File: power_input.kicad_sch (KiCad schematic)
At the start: 47 parts, among them IC10 MAX17263LETD+T, IC2 MCP73871, IC4 TPS2013A, IC7 LP38691-ADJ, J2 JST_4PIN

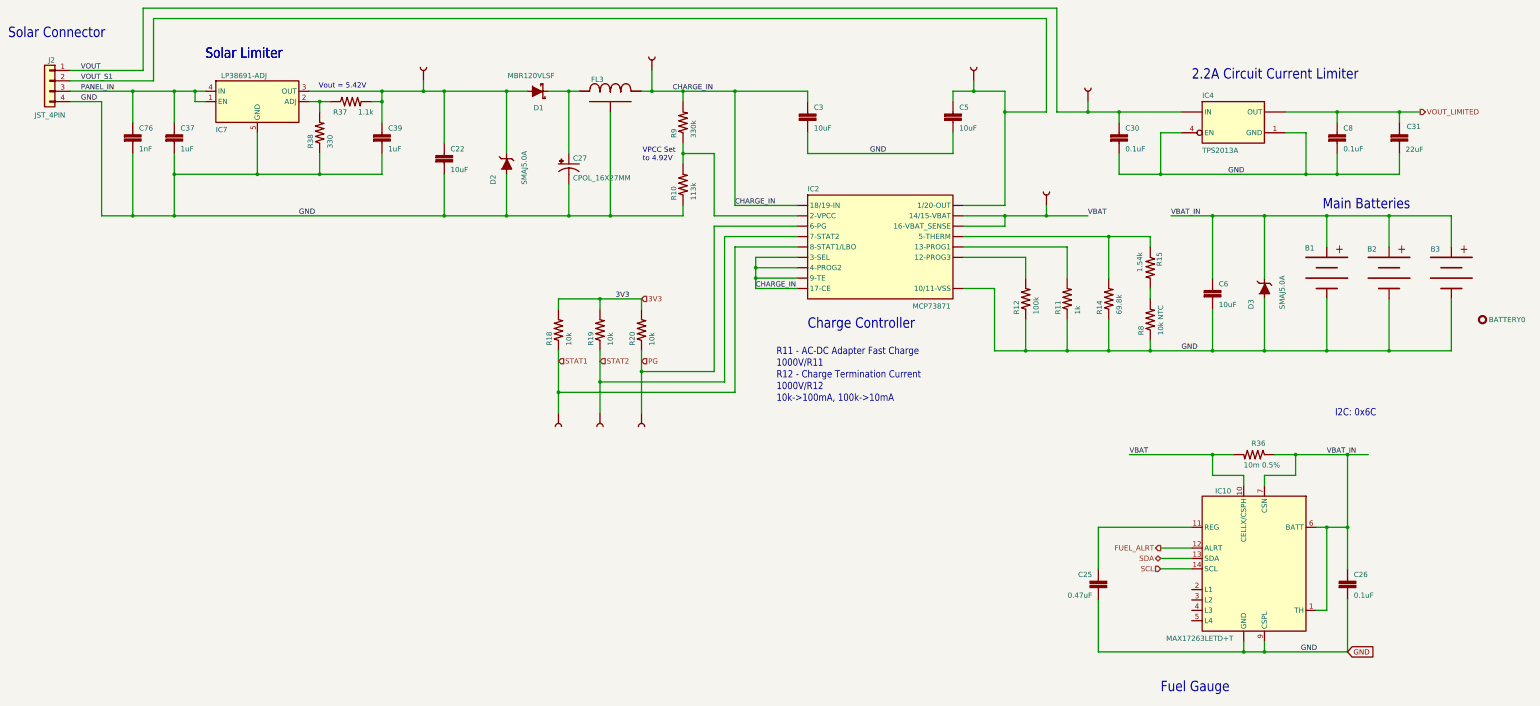
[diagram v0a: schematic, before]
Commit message: name change to Loriques
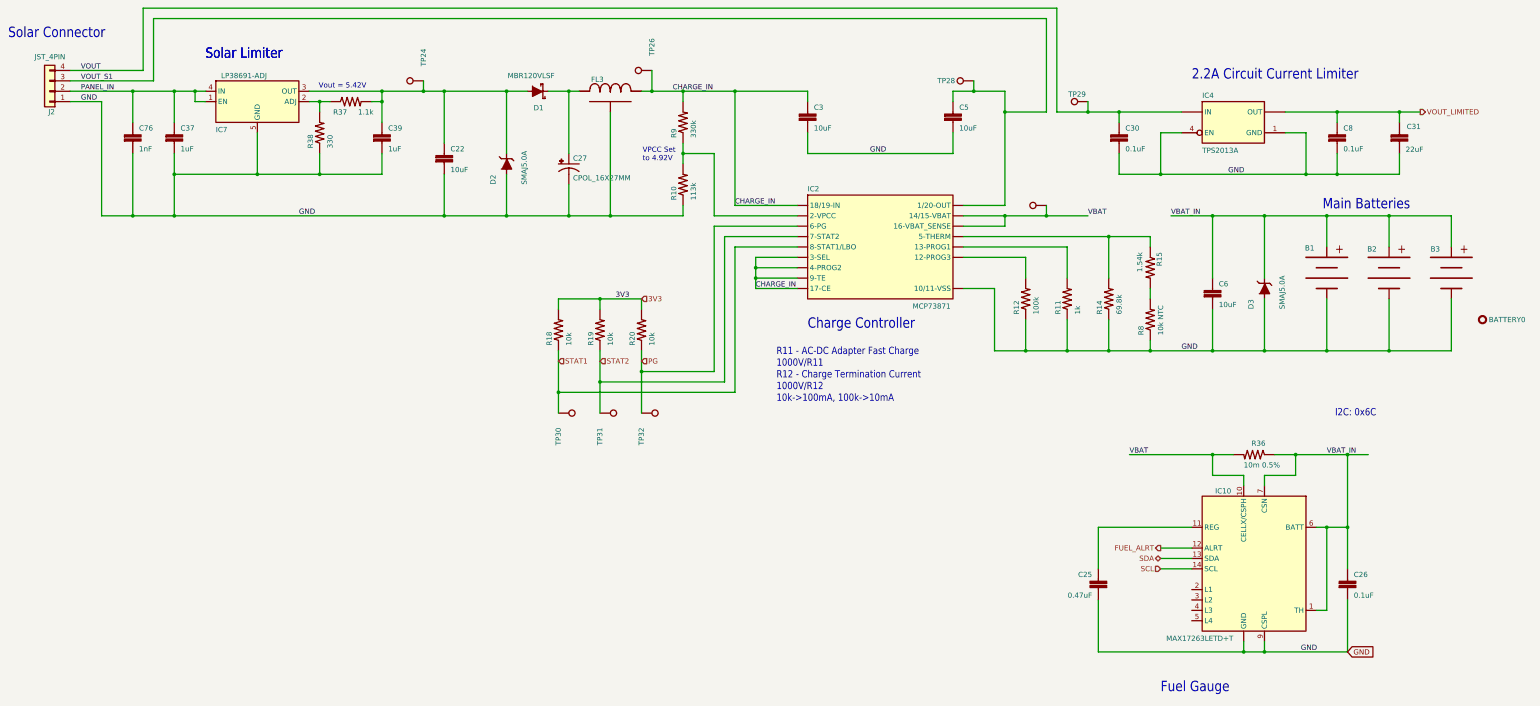
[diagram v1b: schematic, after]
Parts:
- B1, B2, B3: footprint autonode:1042 -> Loriques:1042; symbol autonode:18650_1042 -> Loriques:18650_1042
- BATTERY0: footprint autonode:NOTHING -> Loriques:NOTHING; symbol autonode:BULLET -> Loriques:BULLET
- C22, C3, C5, C6: symbol autonode:CAP0603 -> Loriques:CAP0603
- C25, C26, C30, C37, C39, C76, C8: symbol autonode:CAP0402 -> Loriques:CAP0402
- C27: footprint autonode:25PK4700MEFC16X25 -> Loriques:25PK4700MEFC16X25; symbol autonode:CPOL_16X27MM -> Loriques:CPOL_16X27MM
- C31: symbol autonode:CAP0805 -> Loriques:CAP0805
- D1: footprint autonode:SOD−123FL -> Loriques:SOD−123FL; symbol autonode:MBR120VLSF -> Loriques:MBR120VLSF
- D2, D3: footprint autonode:DO-214AC(SMA) -> Loriques:DO-214AC(SMA); symbol autonode:SMAJ5.0A -> Loriques:SMAJ5.0A
- FL3: footprint autonode:YFF31HC2A104MT000N -> Loriques:YFF31HC2A104MT000N; symbol autonode:YFF31HC2A104MT000N -> Loriques:YFF31HC2A104MT000N
- IC10: footprint autonode:SON40P300X300X80-15T170X230N -> Loriques:SON40P300X300X80-15T170X230N; symbol autonode:MAX17263LETD+T -> Loriques:MAX17263LETD+T
- IC2: footprint autonode:QFN20-ML_4X4MM -> Loriques:QFN20-ML_4X4MM; symbol autonode:MCP73871 -> Loriques:MCP73871
- IC4: footprint autonode:R-PDSO-G8_NOPAD -> Loriques:R-PDSO-G8_NOPAD; symbol autonode:TPS2013A -> Loriques:TPS2013A
- IC7: footprint autonode:SOT-223-5 -> Loriques:SOT-223-5; symbol autonode:LP38691-ADJ -> Loriques:LP38691-ADJ
- J2: footprint autonode:JST-PH-4-SMT -> Loriques:JST-PH-4-SMT
- R10, R11, R12, R14, R15, R18, R19, R20, R37, R38, R8, R9: symbol autonode:RESISTOR0402-RES -> Loriques:RESISTOR0402-RES
- R36: symbol autonode:RESISTOR1206 -> Loriques:RESISTOR1206
- TP24, TP26, TP27, TP28, TP29, TP30, TP31, TP32: footprint autonode:PAD.03X.05 -> TestPoint:TestPoint_Pad_D1.5mm; symbol autonode:TEST-POINT3X5 -> Connector:TestPoint
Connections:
- net CHARGE_IN: now also TP26.1; no longer TP26.0 (1)
- net GND: now also J2.1 (Pin_1); no longer J2.4 (Pin_4)
- net PANEL_IN: now also J2.2 (Pin_2); no longer J2.3 (Pin_3)
- net PG: now also TP32.1; no longer TP32.0 (1)
- net STAT1: now also TP30.1; no longer TP30.0 (1)
- net STAT2: now also TP31.1; no longer TP31.0 (1)
- net VBAT: now also TP27.1; no longer TP27.0 (1)
- net VOUT: now also J2.4 (Pin_4), TP29.1; no longer J2.1 (Pin_1), TP29.0 (1)
- net VOUT_S1: now also J2.3 (Pin_3), TP28.1; no longer J2.2 (Pin_2), TP28.0 (1)
- net at C22.1, C39.1, D1.A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: now also TP24.1; no longer TP24.0 (1)
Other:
- moved on the sheet: J2

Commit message: added logo to schematic sheets
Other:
- title: (none) -> Loriques
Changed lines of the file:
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@@
 	(generator "eeschema")
 	(generator_version "9.0")
-	(paper "User" 411.302 254.991)
+	(paper "A3")
+	(title_block
+		(title "Loriques")
+		(date "2025-07-11")
+		(rev "A")
+	)
 	(text "Vout = 5.42V"
 		(exclude_from_sim no)

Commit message: added lots of 3d models
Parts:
- C27: footprint Loriques:25PK4700MEFC16X25 -> Capacitor_THT:CP_Radial_D16.0mm_P7.50mm; DK (none) -> 1189-1732-ND; PARTNO (none) -> 25PK4700MEFC16X25
- J2: DK (none) -> 455-B4B-PH-SM4-TBCT-ND; PARTNO (none) -> B4B-PH-SM4-TB
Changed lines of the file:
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@@
 			)
 		)
-		(property "Footprint" "Loriques:25PK4700MEFC16X25"
+		(property "Footprint" "Capacitor_THT:CP_Radial_D16.0mm_P7.50mm"
 			(at 154.94 104.14 0)
 			(effects
@@
 		)
 		(property "Description" "4700µF 25V Aluminum Electrolytic Capacitors Radial"
+			(at 154.94 104.14 0)
+			(effects
+				(font
+					(size 1.27 1.27)
+				)
+				(hide yes)
+			)
+		)
+		(property "PARTNO" "25PK4700MEFC16X25"
+			(at 154.94 104.14 0)
+			(effects
+				(font
+					(size 1.27 1.27)
+				)
+				(hide yes)
+			)
+		)
+		(property "DK" "1189-1732-ND"
 			(at 154.94 104.14 0)
 			(effects
@@
 			(at 27.94 86.36 0)
 			(effects
+				(font
+					(size 1.27 1.27)
+				)
+				(hide yes)
+			)
+		)
+		(property "PARTNO" "B4B-PH-SM4-TB"
+			(at 27.94 86.36 0)
+			(effects
+				(font
+					(size 1.27 1.27)
+				)
+				(hide yes)
+			)
+		)
+		(property "DK" "455-B4B-PH-SM4-TBCT-ND"
+			(at 27.94 86.36 0)
+			(effects

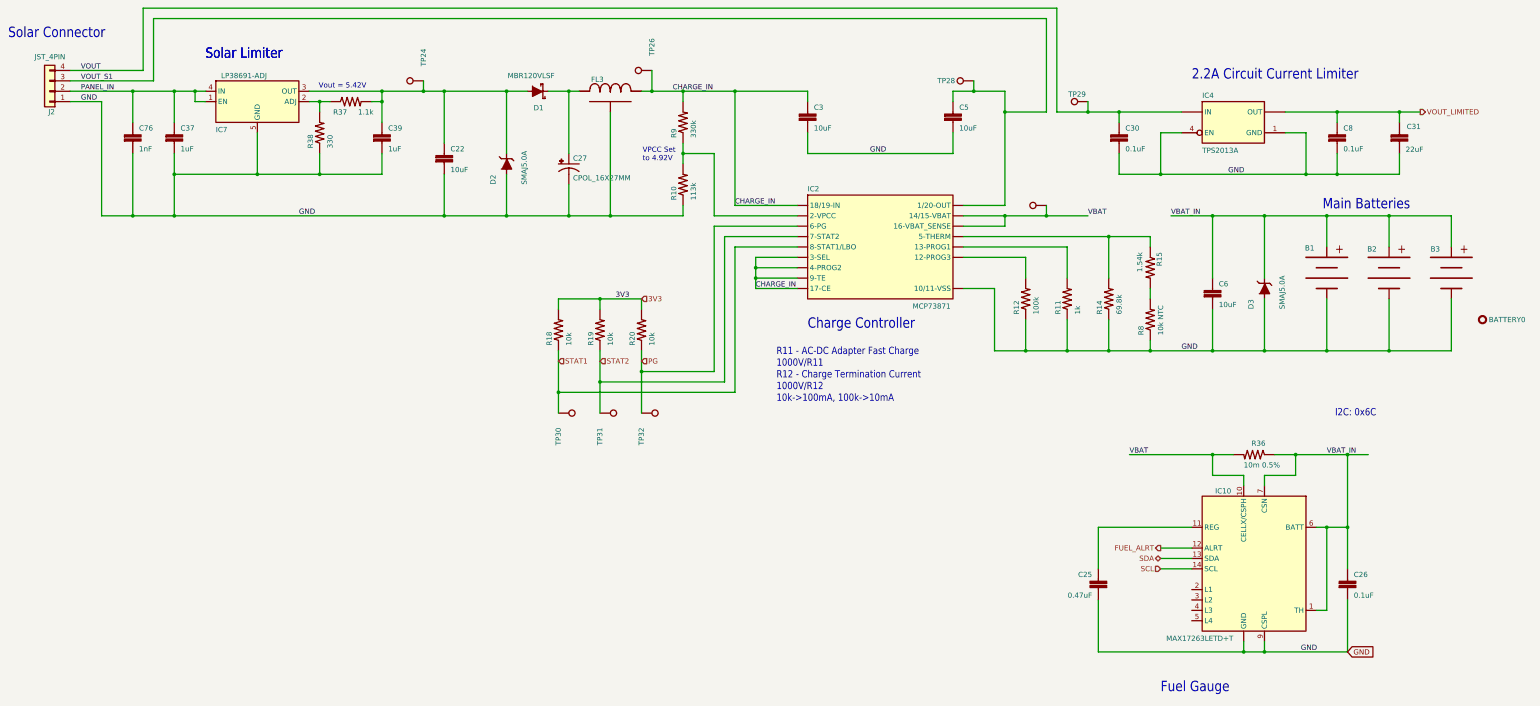
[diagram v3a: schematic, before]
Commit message: more 3D parts. changed out the temp/humidity sensor for an instock one
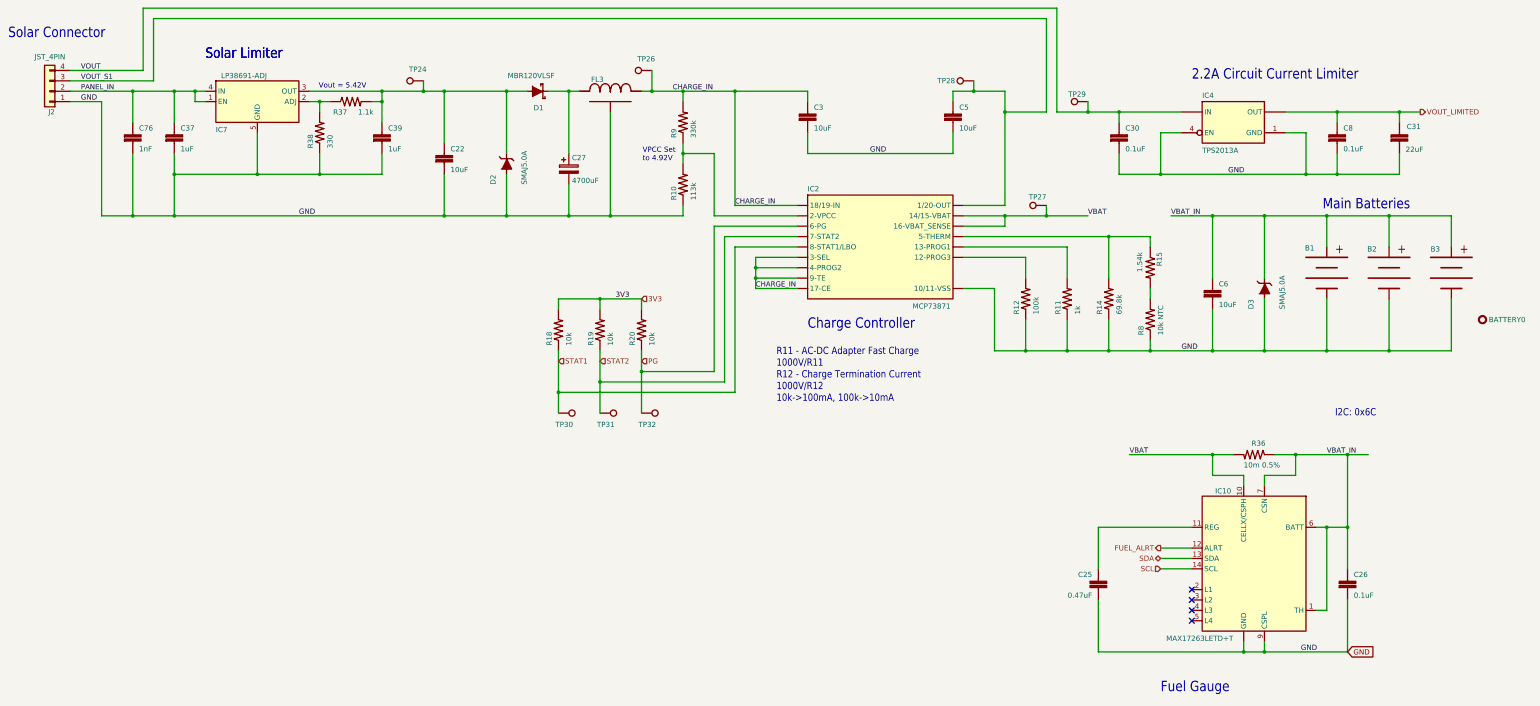
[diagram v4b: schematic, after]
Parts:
- C27: value CPOL_16X27MM -> 4700uF; symbol Loriques:CPOL_16X27MM -> Device:C_Polarized
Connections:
- net GND: now also C27.2; no longer C27.-
- net at D1.K, FL3.1: now also C27.1; no longer C27.+
- no-connect marks 0 -> 4
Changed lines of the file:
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@@
 		(color 0 0 0 0)
 	)
+	(no_connect
+		(at 307.34 215.9)
+	)
+	(no_connect
+		(at 307.34 210.82)
+	)
+	(no_connect
+		(at 307.34 213.36)
+	)
+	(no_connect
+		(at 307.34 208.28)
+	)
 	(wire
 		(pts
@@
 		(dnp no)
 		(property "Reference" "TP27"
-			(at 272.542 110.744 0)
+			(at 271.78 111.506 90)
 			(effects
 				(font
@@
 				)
 				(justify left bottom)
-				(hide yes)
 			)
 		)
@@
 		(dnp no)
 		(property "Reference" "TP32"
-			(at 171.958 168.656 0)
+			(at 171.958 168.656 90)
 			(effects
 				(font
@@
 	)
 	(symbol
-		(lib_id "Loriques:CPOL_16X27MM")
-		(at 154.94 104.14 0)
+		(lib_id "Device:C_Polarized")
+		(at 154.94 105.41 0)
 		(unit 1)
 		(exclude_from_sim no)
@@
 		(dnp no)
 		(property "Reference" "C27"
-			(at 155.956 103.505 0)
+			(at 155.702 103.378 0)
 			(effects
 				(font
@@
 			)
 		)
-		(property "Value" "CPOL_16X27MM"
-			(at 155.956 108.331 0)
+		(property "Value" "4700uF"
+			(at 155.702 108.966 0)
 			(effects
 				(font
@@
 		)
 		(property "Footprint" "Capacitor_THT:CP_Radial_D16.0mm_P7.50mm"
-			(at 154.94 104.14 0)
+			(at 155.9052 109.22 0)
 			(effects
 				(font
@@
 			)
 		)
-		(property "Datasheet" ""
-			(at 154.94 104.14 0)
+		(property "Datasheet" "~"
+			(at 154.94 105.41 0)
 			(effects
 				(font
@@
 			)
 		)
-		(property "Description" "4700µF 25V Aluminum Electrolytic Capacitors Radial"
-			(at 154.94 104.14 0)
+		(property "Description" "Polarized capacitor"
+			(at 154.94 105.41 0)
 			(effects
 				(font
@@
 		)
 		(property "PARTNO" "25PK4700MEFC16X25"
-			(at 154.94 104.14 0)
+			(at 154.94 105.41 0)
 			(effects
 				(font
@@
 		)
 		(property "DK" "1189-1732-ND"
-			(at 154.94 104.14 0)
+			(at 154.94 105.41 0)
 			(effects
 				(font
@@
 			)
 		)
-		(pin "+"
+		(pin "1"
 		)
-		(pin "-"
+		(pin "2"
 		)
 		(instances
@@
 		(dnp no)
 		(property "Reference" "TP31"
-			(at 161.798 168.656 0)
+			(at 161.798 168.656 90)
 			(effects
 				(font
@@
 		(dnp no)
 		(property "Reference" "TP26"
-			(at 176.022 77.724 0)
+			(at 176.022 77.724 90)
 			(effects
 				(font
@@
 		(dnp no)
 		(property "Reference" "TP30"
-			(at 151.638 168.656 0)
+			(at 151.638 168.656 90)
 			(effects
 				(font
@@
 		(dnp no)
 		(property "Reference" "TP24"
-			(at 120.142 80.264 0)
+			(at 120.142 80.264 90)
 			(effects
 				(font

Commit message: lots of routing, tweaking placement. adding courtyards
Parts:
- D2, D3: footprint Loriques:DO-214AC(SMA) -> Diode_SMD:D_SMA; symbol Loriques:SMAJ5.0A -> Device:D_Zener_Filled; DK (none) -> SMAJ5.0ALFCT-ND; PARTNO (none) -> SMAJ5.0A
- IC10: DK (none) -> 175-MAX17263LETD+TCT-ND; PARTNO (none) -> MAX17263LETD+T
- IC2: DK (none) -> MCP73871-2CCI/ML-ND; PARTNO (none) -> MCP73871-2CCI/ML
- IC4: DK (none) -> 296-2558-5-ND; PARTNO (none) -> TPS2013AD
- IC7: DK (none) -> LP38693MP-ADJ/NOPBCT-ND; PARTNO (none) -> LP38693MP-ADJ/NOPB
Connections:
- net GND: now also D2.1 (K), D3.1 (K); no longer D2.A, D3.A
- net VBAT_IN: now also D3.2 (A); no longer D3.K
- net at C22.1, C39.1, D1.A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: now also D2.2 (A); no longer D2.K
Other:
- moved on the sheet: D3

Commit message: initial routing done!
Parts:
- D1: DK (none) -> MBR120VLSFT1GOSCT-ND; PARTNO (none) -> MBR120VLSFT1G
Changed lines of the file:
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@@
 			)
 		)
-		(property "Datasheet" ""
+		(property "Datasheet" "https://www.onsemi.com/pdf/datasheet/mbr120vlsft1-d.pdf"
 			(at 147.32 86.36 0)
 			(effects
@@
 			(effects
 				(font
+					(size 1.27 1.27)
+				)
+				(hide yes)
+			)
+		)
+		(property "PARTNO" "MBR120VLSFT1G"
+			(at 146.558 92.964 0)
+			(effects
+				(font
+					(size 1.27 1.27)
+				)
+				(hide yes)
+			)
+		)
+		(property "DK" "MBR120VLSFT1GOSCT-ND"
+			(at 146.558 92.964 0)
+			(effects
+				(font
